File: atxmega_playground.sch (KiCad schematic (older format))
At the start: 98 parts

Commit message: Begin assigning footprints
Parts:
- removed U?: AD5280, symbol AD5280
- CON1: renamed from CON?; footprint AVR-PDI-6 -> (none)
- IC1: renamed from IC?; footprint TQFP44 -> (none)
- P1: renamed from P?; footprint (none) -> Connect:USB_Mini-B
- U12, U13: renamed from U?; footprint (none) -> Housings_SOIC:SOIC-16_3.9x9.9mm_Pitch1.27mm
- U2: renamed from U?; footprint (none) -> TO_SOT_Packages_SMD:SOT-223
- U3: renamed from U?; footprint (none) -> Housings_SSOP:TSSOP-24_4.4x7.8mm_Pitch0.65mm
- U4: renamed from U?; footprint (none) -> Housings_SOIC:SOIC-18W_7.5x11.6mm_Pitch1.27mm
- U7: renamed from U?; footprint (none) -> TO_SOT_Packages_SMD:SOT-23-6
- gave numbers to parts that had none: 88
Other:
- note removed: "Ideas"

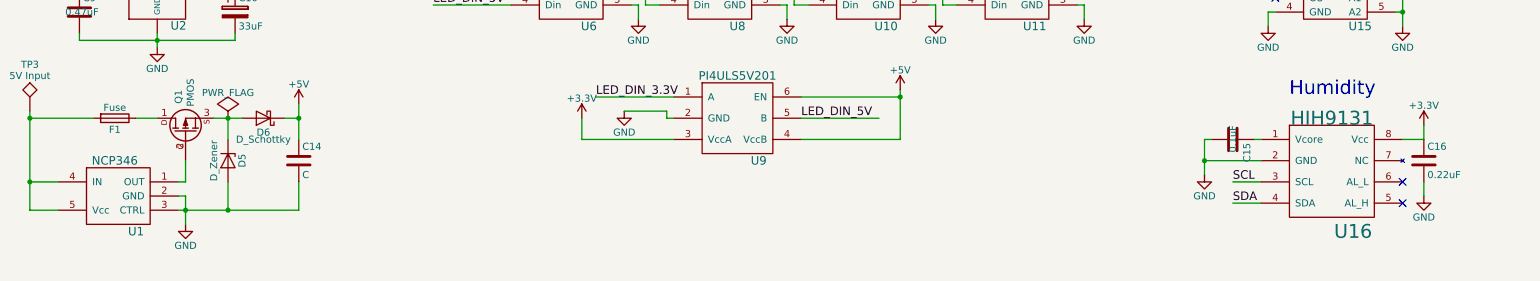
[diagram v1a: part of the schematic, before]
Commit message: More footprints, beginning stages of layout
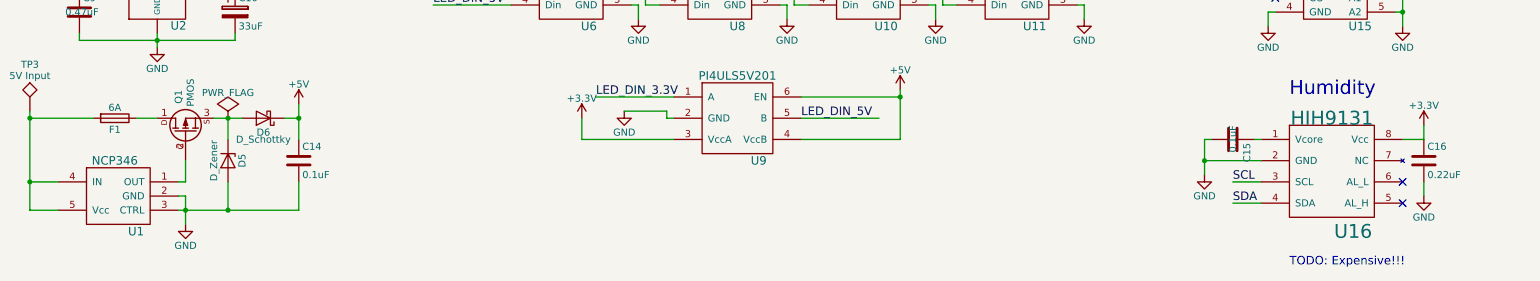
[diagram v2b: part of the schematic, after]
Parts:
- C1, C11, C12, C13, C15, C16, C2, C3, C4, C5, C6, C7, C8, C9: footprint (none) -> atxmega:C_0805
- C14: value C -> 0.1uF; footprint (none) -> atxmega:C_0805
- CON1: footprint (none) -> Pin_Headers:Pin_Header_Straight_2x03_Pitch2.54mm
- D1, D10, D11, D12, D2, D3, D4, D7, D8, D9: footprint (none) -> atxmega:LED_0805
- F1: value Fuse -> 6A; footprint (none) -> atxmega:R_1206
- IC1: footprint (none) -> Housings_QFP:TQFP-44_10x10mm_Pitch0.8mm
- P1: footprint Connect:USB_Mini-B -> Connectors:USB_Mini-B
- P2, P3: footprint (none) -> Pin_Headers:Pin_Header_Straight_1x02_Pitch2.54mm
- P4: footprint (none) -> Pin_Headers:Pin_Header_Straight_1x08_Pitch2.54mm
- P5, S1: footprint (none) -> Pin_Headers:Pin_Header_Straight_1x03_Pitch2.54mm
- P6, P7: footprint (none) -> Pin_Headers:Pin_Header_Straight_1x04_Pitch2.54mm
- Q1, Q2, Q3, Q4: footprint cuauv:SOT-23-3 -> atxmega:SOT-23-5
- R1, R10, R11, R12, R13, R14, R15, R16, R17, R18, R19, R2, R20, R21, R22, R23, R24, R25, R26, R27, R28, R29, R3, R30, R31, R4, R5, R6, R7, R8, R9: footprint (none) -> atxmega:R_0805
- U1, U5: footprint (none) -> atxmega:SOT-23-5
- U10, U11, U6, U8: footprint (none) -> atxmega:WS2812B
- U14, U16: footprint (none) -> Housings_SOIC:SOIC-8_3.9x4.9mm_Pitch1.27mm
- U15: footprint (none) -> atxmega:TSSOP-8_4.4x3mm_Pitch0.65mm
- Y1: footprint (none) -> Crystals:Crystal_HC49-U_Vertical
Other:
- note added: "TODO: Expensive!!!"

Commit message: Add GPIO's ADC and 5V sensors, 7seg display footprint, and HIM's IMU's
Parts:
- removed U15: LM75BD, atxmega:TSSOP-8_4.4x3mm_Pitch0.65mm, symbol LM75BD
- removed U16: HIH9131, Housings_SOIC:SOIC-8_3.9x4.9mm_Pitch1.27mm, symbol HIH9131
- added C17: 1uF, atxmega:c_elec_18x21.5, symbol CP
- added C18, C20, C21, C25, C27, C28, C29, C30: 0.1uF, atxmega:C_0805, symbol C
- added C19: 10uF, atxmega:C_0805, symbol C
- added C22, C23: 4pF, atxmega:C_0805, symbol C
- added C24: C, atxmega:C_0805, symbol C
- added C26: 47pF, atxmega:C_0805, symbol C
- added C31: 2.2nF, atxmega:C_0805, symbol C
- added IMU1: KMX62-1031, atxmega:KXG03_footprint, symbol KMX62-1031
- added IMU2: KXG03, atxmega:KXG03_footprint, symbol KXG03
- added P8: CONN_01X07, symbol CONN_01X07
- added R32, R33, R34: 1k, atxmega:R_0805, symbol R
- added R35: 51k, atxmega:R_0805, symbol R
- added U15: REF195, Housings_SOIC:SOIC-8_3.9x4.9mm_Pitch1.27mm, symbol REF195
- added U16: AD7708, Housings_SOIC:SOIC-28W_7.5x17.9mm_Pitch1.27mm, symbol AD7708
- added U17: MPXH6101A, atxmega:SOIC-8_7.5x7.5mm_Pitch1.27mm, symbol MPXH6101A
- added U18: LM35, Housings_SOIC:SOIC-8_3.9x4.9mm_Pitch1.27mm, symbol LM35
- added Y2: 32.768kHz, atxmega:R_0805, symbol Crystal
- AFF1, AFF2: footprint (none) -> atxmega:7seg_SC56-11SRWA
- C15: value 0.1uF -> 10uF
- C16: value 0.22uF -> 0.1uF
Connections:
- net labels added: +12V, ADC4, ADC5, ADC6, ADC_RDY, ADC_RESET, IMU_INT1, IMU_INT2, MC_ADC1, MC_ADC2, MC_ADC3, Vpressure, Vtemp, ~ADC_CS
- wire segments 399 -> 494
- no-connect marks 24 -> 31
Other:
- note added: "5V ADC Sensors"
- note added: "ADC"
- note added: "IMUs"
- note removed: "Humidity"
- note removed: "Sensors"
- note removed: "TODO: Expensive!!!"
- note removed: "Temperature"
- moved on the sheet: D10, D11, D12, R29, R30, R31, U14

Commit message: Basic layout, component positions mostly final
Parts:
- removed P4: CONN_01X08, Pin_Headers:Pin_Header_Straight_1x08_Pitch2.54mm, symbol CONN_01X08
- removed R32, R33, R34: 1k, atxmega:R_0805, symbol R
- added P4: CONN_01X06, symbol CONN_01X06
- added TP4, TP?: TEST, atxmega:TESTPOINT, symbol TEST
- C17: footprint atxmega:c_elec_18x21.5 -> (none)
- C24: value C -> 0.1uF
- D6: footprint (none) -> atxmega:R_0805
- P8: footprint (none) -> Pin_Headers:Pin_Header_Straight_1x07_Pitch2.54mm
- Q1, Q2, Q3, Q4: footprint atxmega:SOT-23-5 -> atxmega:SOT-23-3_Handsoldering
- TP3: footprint (none) -> atxmega:TESTPOINT
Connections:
- net labels removed: GPIO6, GPIO7, SR_RSCLK

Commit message: Initial layout complete, no DRC errors or unconnected tracks
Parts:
- removed P2: CONN_01X02, Pin_Headers:Pin_Header_Straight_1x02_Pitch2.54mm, symbol CONN_01X02
- removed P6: CONN_01X04, Pin_Headers:Pin_Header_Straight_1x04_Pitch2.54mm, symbol CONN_01X04
- removed P8: CONN_01X07, Pin_Headers:Pin_Header_Straight_1x07_Pitch2.54mm, symbol CONN_01X07
- added D13, D14, D15: LED, atxmega:LED_0805, symbol LED
- added P2: CONN_01X05, Pin_Headers:Pin_Header_Straight_1x05_Pitch2.54mm, symbol CONN_01X05
- added R32, R33, R34: R, atxmega:R_0805, symbol R
- D5: footprint (none) -> atxmega:SOD-123
- L1: footprint (none) -> atxmega:R_0805
- TP1, TP2: footprint (none) -> atxmega:TESTPOINT
- U9: footprint (none) -> atxmega:SOT-23-6
- gave numbers to parts that had none: 1
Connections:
- net labels added: LED4, LED5, LED6
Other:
- moved on the sheet: P7

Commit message: First revision, finalized!
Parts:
- removed P4: CONN_01X06, symbol CONN_01X06
- C10, C17: footprint (none) -> atxmega:R_1206
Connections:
- net labels removed: ADC5, ADC6, GPIO1, GPIO2, GPIO3, GPIO4, GPIO5, IMU_INT1, IMU_INT2, MC_ADC1, MC_ADC2, MC_ADC3
- wire segments 494 -> 481
- no-connect marks 31 -> 41
